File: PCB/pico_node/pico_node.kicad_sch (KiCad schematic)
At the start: 19 parts, among them J1 INMP441, J2 NEO-6M, J3 MD-CD42, J4 RESET_POWER_SW, J5 UART0_DEBUG, J6 UART1_DEBUG, J7 BATTERY, J8 BUCK_5V, Q1 BC547, U1 NRF24L01_Breakout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

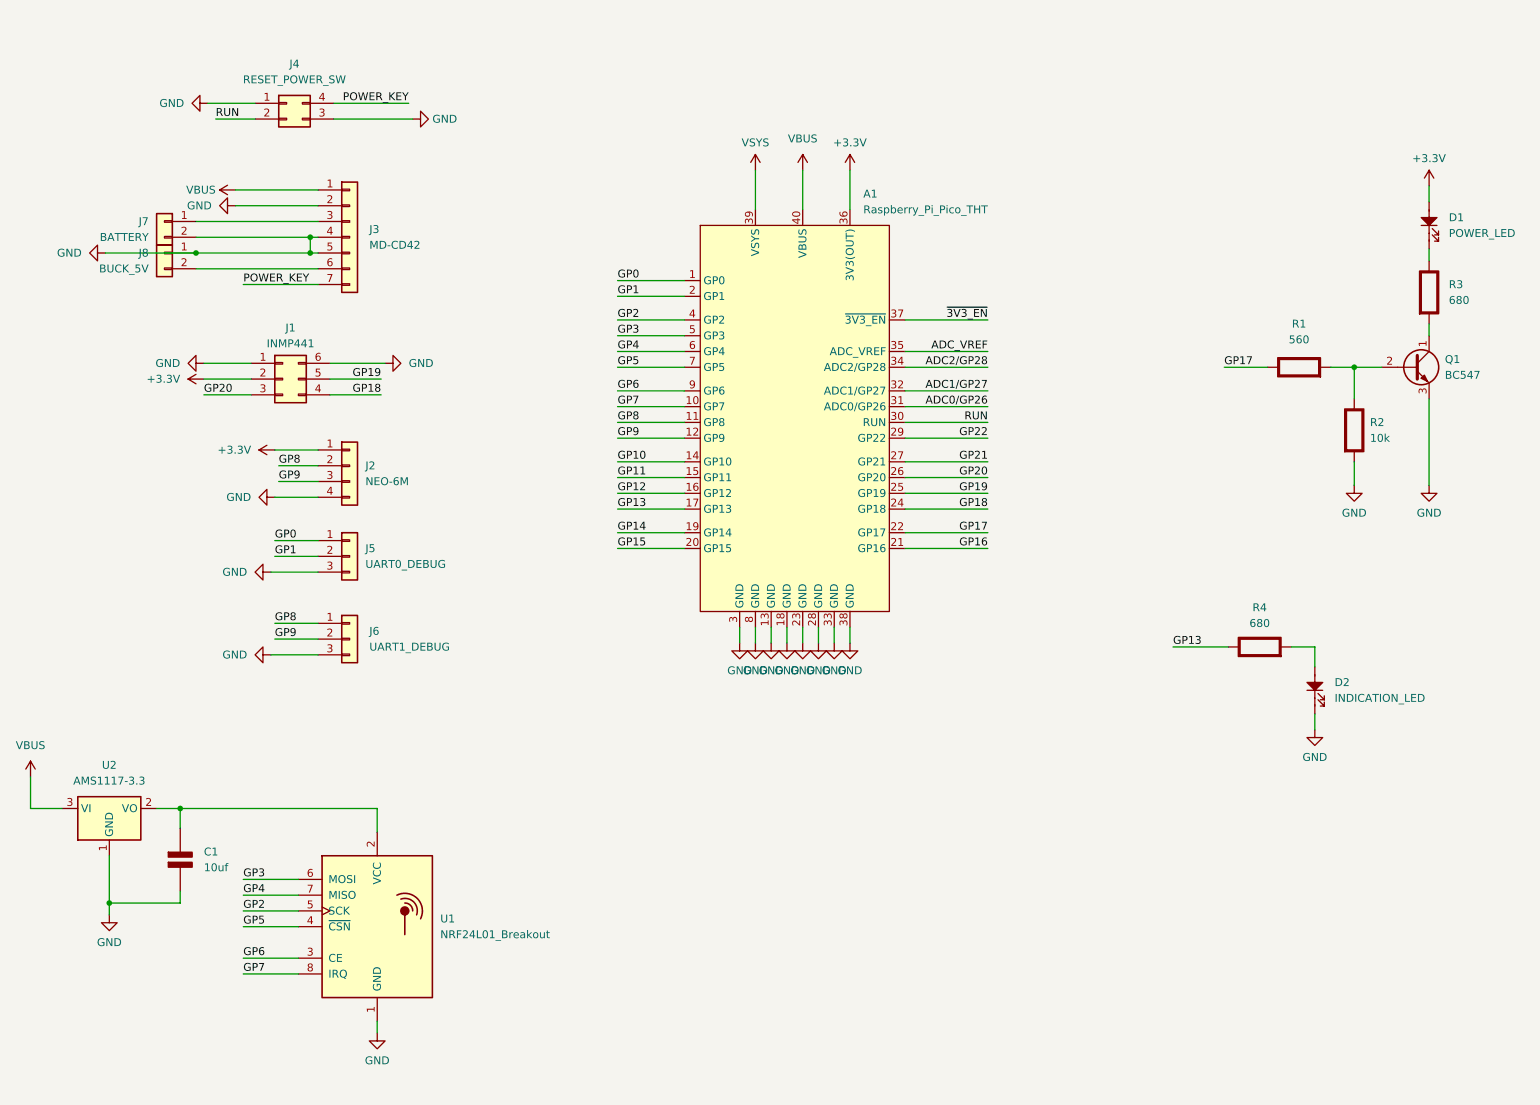
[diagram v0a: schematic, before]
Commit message: updated ML model using Edge impulse updated INMP441 pio code
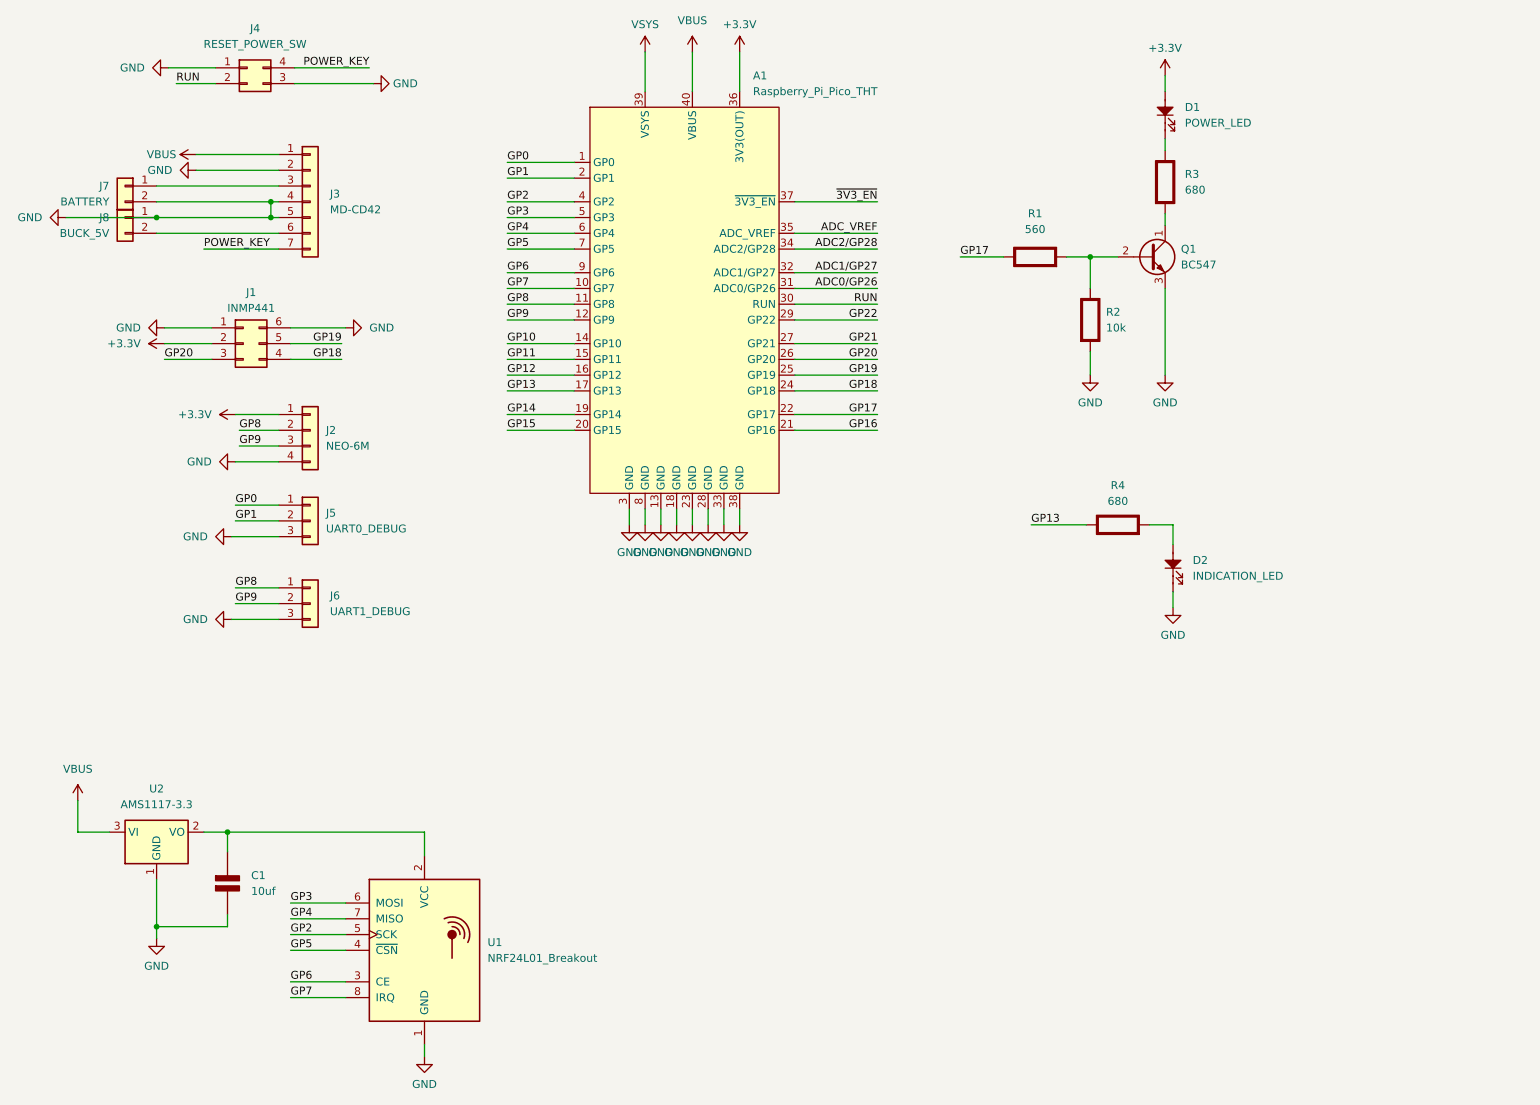
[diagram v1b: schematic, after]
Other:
- company: (none) -> RV College of Engineering
- title: (none) -> IDP Project Sensor Node 
- moved on the sheet: A1, C1, D1, D2, J1, J2, J3, J4, J5, J6, J7, J8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
